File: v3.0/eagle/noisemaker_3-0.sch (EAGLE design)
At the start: 57 parts, among them IC1 REG1117, U3 ATMEGA32U4, Y1 16MHz

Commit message: board updates...
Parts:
- NPN: device transistor:-NPN-TO220V -> SparkFun-DiscreteSemi:TRANSISTOR_NPNSOT23-3
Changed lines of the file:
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@@
 <part name="R8" library="SparkFun-Passives" deviceset="RESISTOR" device="1206"/>
 <part name="R9" library="SparkFun-Passives" deviceset="RESISTOR" device="1206"/>
-<part name="NPN" library="transistor" deviceset="*-NPN-" device="TO220V"/>
+<part name="NPN" library="SparkFun-DiscreteSemi" deviceset="TRANSISTOR_NPN" device="SOT23-3"/>
 <part name="GND16" library="supply1" deviceset="GND" device=""/>
 <part name="AMP-" library="SparkFun-Connectors" deviceset="M01" device="PTH_LONGPAD"/>

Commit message: updated board layout
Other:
- moved on the sheet: AMP+, AMP-, JP4, NPN, PH1, PH2, PH3, R11, R15, R19, R20, R3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

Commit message: updated board layout tues
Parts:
- added JP8: M01PTH_LONGPAD, SparkFun-Connectors:M01PTH_LONGPAD
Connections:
- net VCC: now also JP8.1
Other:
- note added: "sensor1"
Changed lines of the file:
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@@
 <part name="P+12" library="SparkFun" deviceset="3.3V" device="" value="VCC"/>
 <part name="P+14" library="SparkFun" deviceset="3.3V" device="" value="VCC"/>
+<part name="JP8" library="SparkFun-Connectors" deviceset="M01" device="PTH_LONGPAD" value="M01PTH_LONGPAD"/>
 </parts>
 <sheets>
@@
 <text x="220.98" y="27.94" size="1.778" layer="94" ratio="10">power</text>
 <text x="263.144" y="174.752" size="1.778" layer="94">Gadgiteration Noisemaker v3.0</text>
+<text x="205.74" y="154.94" size="1.778" layer="94">sensor1</text>
+<text x="205.74" y="152.4" size="1.778" layer="94">sensor1</text>
+<text x="205.74" y="149.86" size="1.778" layer="94">sensor1</text>
 </plain>
 <instances>
@@
 <attribute name="VALUE" x="40.64" y="47.244" size="1.778" layer="96" rot="R180"/>
 </instance>
+<instance part="JP8" gate="G$1" x="114.3" y="162.56" rot="R180"/>
 </instances>
 <busses>
@@
 <wire x1="68.58" y1="154.94" x2="68.58" y2="162.56" width="0.1524" layer="91"/>
 <junction x="68.58" y="162.56"/>
-</segment>
-<segment>
+<pinref part="JP8" gate="G$1" pin="1"/>
+<wire x1="106.68" y1="162.56" x2="99.06" y2="162.56" width="0.1524" layer="91"/>
+</segment>
+<segment>

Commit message: merging in @shanqiu's latest updates
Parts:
- removed PH3: M9960_11B, photo-elements:M9960_11B
- removed R20: (no value), SparkFun-Passives:RESISTOR1206
- added JP9, LED_STRIP: (no value), pinhead:PINHD-1X3/90
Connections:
- new net N$11: LED_STRIP.3
- new net N$6: LED_STRIP.1
- net A4: now also JP9.2; no longer PH3.2, R20.2
- net D6: now also LED_STRIP.2
- net GND: now also JP9.3; no longer R20.1
- net VCC: now also JP9.1; no longer PH3.1
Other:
- note added: "audio"
- note added: "human circuit pole"
- note added: "led"
- note added: "led _strip"
- note added: "leds(human circuit/ regular circuit)"
- note added: "mode button"
- note added: "range button"
- note added: "regular circuit pole"
- note added: "sensor1(2 legs)"
- note added: "sensor2(2 legs)"
- note added: "sensor3(3 legs)"
- note removed: "sensor1"
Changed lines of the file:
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@@
 <?xml version="1.0" encoding="utf-8"?>
 <!DOCTYPE eagle SYSTEM "eagle.dtd">
-<eagle version="6.4">
+<eagle version="6.5.0">
 <drawing>
 <settings>
@@
 <part name="R15" library="SparkFun-Passives" deviceset="RESISTOR" device="1206"/>
 <part name="R19" library="SparkFun-Passives" deviceset="RESISTOR" device="1206"/>
-<part name="R20" library="SparkFun-Passives" deviceset="RESISTOR" device="1206"/>
 <part name="PH2" library="photo-elements" deviceset="M9960_11" device="" technology="B"/>
-<part name="PH3" library="photo-elements" deviceset="M9960_11" device="" technology="B"/>
 <part name="GND21" library="supply1" deviceset="GND" device=""/>
 <part name="P+3" library="SparkFun" deviceset="3.3V" device="" value="VCC"/>
@@
 <part name="P+14" library="SparkFun" deviceset="3.3V" device="" value="VCC"/>
 <part name="JP8" library="SparkFun-Connectors" deviceset="M01" device="PTH_LONGPAD" value="M01PTH_LONGPAD"/>
+<part name="JP9" library="pinhead" deviceset="PINHD-1X3" device="/90"/>
+<part name="LED_STRIP" library="pinhead" deviceset="PINHD-1X3" device="/90"/>
+<part name="GND13" library="SparkFun" deviceset="GND" device=""/>
+<part name="P+8" library="SparkFun" deviceset="3.3V" device="" value="VCC"/>
 </parts>
 <sheets>
@@
 <text x="220.98" y="27.94" size="1.778" layer="94" ratio="10">power</text>
 <text x="263.144" y="174.752" size="1.778" layer="94">Gadgiteration Noisemaker v3.0</text>
-<text x="205.74" y="154.94" size="1.778" layer="94">sensor1</text>
-<text x="205.74" y="152.4" size="1.778" layer="94">sensor1</text>
-<text x="205.74" y="149.86" size="1.778" layer="94">sensor1</text>
+<text x="205.74" y="147.32" size="1.778" layer="94">sensor3(3 legs)</text>
+<text x="205.74" y="152.4" size="1.778" layer="94">sensor1(2 legs)</text>
+<text x="205.74" y="149.86" size="1.778" layer="94">sensor2(2 legs)</text>
+<text x="205.74" y="154.94" size="1.778" layer="94">human circuit pole</text>
+<text x="205.74" y="157.48" size="1.778" layer="94">regular circuit pole</text>
+<text x="205.74" y="129.54" size="1.778" layer="94">mode button</text>
+<text x="205.74" y="124.46" size="1.778" layer="94">range button</text>
+<text x="205.74" y="114.3" size="1.778" layer="94">audio</text>
+<text x="205.74" y="116.84" size="1.778" layer="94">leds(human circuit/ regular circuit)</text>
+<text x="205.74" y="96.52" size="1.778" layer="94">led</text>
+<text x="205.74" y="119.38" size="1.778" layer="94">led _strip</text>
+<text x="198.12" y="86.36" size="1.778" layer="94">led</text>
 </plain>
 <instances>
@@
 <instance part="R15" gate="G$1" x="243.84" y="116.84"/>
 <instance part="R19" gate="G$1" x="243.84" y="111.76"/>
-<instance part="R20" gate="G$1" x="243.84" y="106.68"/>
 <instance part="PH2" gate="G$1" x="274.32" y="121.92"/>
-<instance part="PH3" gate="G$1" x="297.18" y="116.84"/>
 <instance part="GND21" gate="1" x="233.68" y="137.16" rot="R180"/>
 <instance part="P+3" gate="G$1" x="109.22" y="60.96" smashed="yes" rot="R270">
@@
 </instance>
 <instance part="JP8" gate="G$1" x="114.3" y="162.56" rot="R180"/>
+<instance part="JP9" gate="A" x="304.8" y="106.68"/>
+<instance part="LED_STRIP" gate="A" x="274.32" y="78.74"/>
+<instance part="GND13" gate="1" x="241.3" y="76.2" rot="R270"/>
+<instance part="P+8" gate="G$1" x="243.84" y="81.28" smashed="yes" rot="R90">
+<attribute name="VALUE" x="237.998" y="78.994" size="1.778" layer="96" rot="R90"/>
+</instance>
 </instances>
 <busses>
@@
 </segment>
 <segment>
-<pinref part="R20" gate="G$1" pin="1"/>
-<wire x1="238.76" y1="106.68" x2="233.68" y2="106.68" width="0.1524" layer="91"/>
-<wire x1="233.68" y1="106.68" x2="233.68" y2="111.76" width="0.1524" layer="91"/>
 <pinref part="R19" gate="G$1" pin="1"/>
 <wire x1="233.68" y1="111.76" x2="233.68" y2="116.84" width="0.1524" layer="91"/>
@@
 <junction x="233.68" y="116.84"/>
 <pinref part="GND21" gate="1" pin="GND"/>
+<pinref part="JP9" gate="A" pin="3"/>
+<wire x1="233.68" y1="104.14" x2="233.68" y2="111.76" width="0.1524" layer="91"/>
+<wire x1="302.26" y1="104.14" x2="233.68" y2="104.14" width="0.1524" layer="91"/>
 </segment>
 <segment>
@@
 <segment>
 <pinref part="PH1" gate="G$1" pin="1"/>
-<pinref part="PH3" gate="G$1" pin="1"/>
 <wire x1="251.46" y1="132.08" x2="274.32" y2="132.08" width="0.1524" layer="91"/>
 <wire x1="274.32" y1="132.08" x2="297.18" y2="132.08" width="0.1524" layer="91"/>
-<wire x1="297.18" y1="132.08" x2="297.18" y2="121.92" width="0.1524" layer="91"/>
 <pinref part="PH2" gate="G$1" pin="1"/>
 <wire x1="274.32" y1="127" x2="274.32" y2="132.08" width="0.1524" layer="91"/>
 <junction x="274.32" y="132.08"/>
 <pinref part="P+7" gate="G$1" pin="3.3V"/>
+<pinref part="JP9" gate="A" pin="1"/>
+<wire x1="302.26" y1="109.22" x2="297.18" y2="109.22" width="0.1524" layer="91"/>
+<wire x1="297.18" y1="109.22" x2="297.18" y2="132.08" width="0.1524" layer="91"/>
 </segment>
 <segment>
@@
 </segment>
 <segment>
-<pinref part="R20" gate="G$1" pin="2"/>
-<wire x1="248.92" y1="106.68" x2="297.18" y2="106.68" width="0.1524" layer="91"/>
-<pinref part="PH3" gate="G$1" pin="2"/>
-<wire x1="297.18" y1="106.68" x2="307.34" y2="106.68" width="0.1524" layer="91"/>
-<wire x1="297.18" y1="111.76" x2="297.18" y2="106.68" width="0.1524" layer="91"/>
-<junction x="297.18" y="106.68"/>
-<label x="302.26" y="106.68" size="1.778" layer="95"/>
+<wire x1="302.26" y1="106.68" x2="314.96" y2="106.68" width="0.1524" layer="91"/>
+<label x="314.96" y="106.68" size="1.778" layer="95"/>
+<pinref part="JP9" gate="A" pin="2"/>
 </segment>
 </net>
@@
 <pinref part="U3" gate="G$1" pin="PD7(ADC10)"/>
 </segment>
+<segment>
+<pinref part="LED_STRIP" gate="A" pin="2"/>
+<wire x1="271.78" y1="78.74" x2="246.38" y2="78.74" width="0.1524" layer="91"/>
+<label x="246.38" y="78.74" size="1.778" layer="95"/>
+</segment>
 </net>
 <net name="D7" class="0">
@@
 <wire x1="162.56" y1="20.32" x2="149.86" y2="20.32" width="0.1524" layer="91"/>
 <junction x="162.56" y="20.32"/>
-<label x="144.78" y="20.32" size="1.778" layer="95"/>
+<label x="142.24" y="20.32" size="1.778" layer="95"/>
 </segment>
 </net>
@@
 </segment>
 </net>
+<net name="N$6" class="0">
+<segment>
+<pinref part="LED_STRIP" gate="A" pin="1"/>
+<wire x1="271.78" y1="81.28" x2="243.84" y2="81.28" width="0.1524" layer="91"/>
+</segment>
+</net>
+<net name="N$11" class="0">
+<segment>
+<pinref part="LED_STRIP" gate="A" pin="3"/>
+<wire x1="271.78" y1="76.2" x2="243.84" y2="76.2" width="0.1524" layer="91"/>
+<pinref part="GND13" gate="1" pin="GND"/>
+<junction x="243.84" y="76.2"/>
+</segment>
+</net>

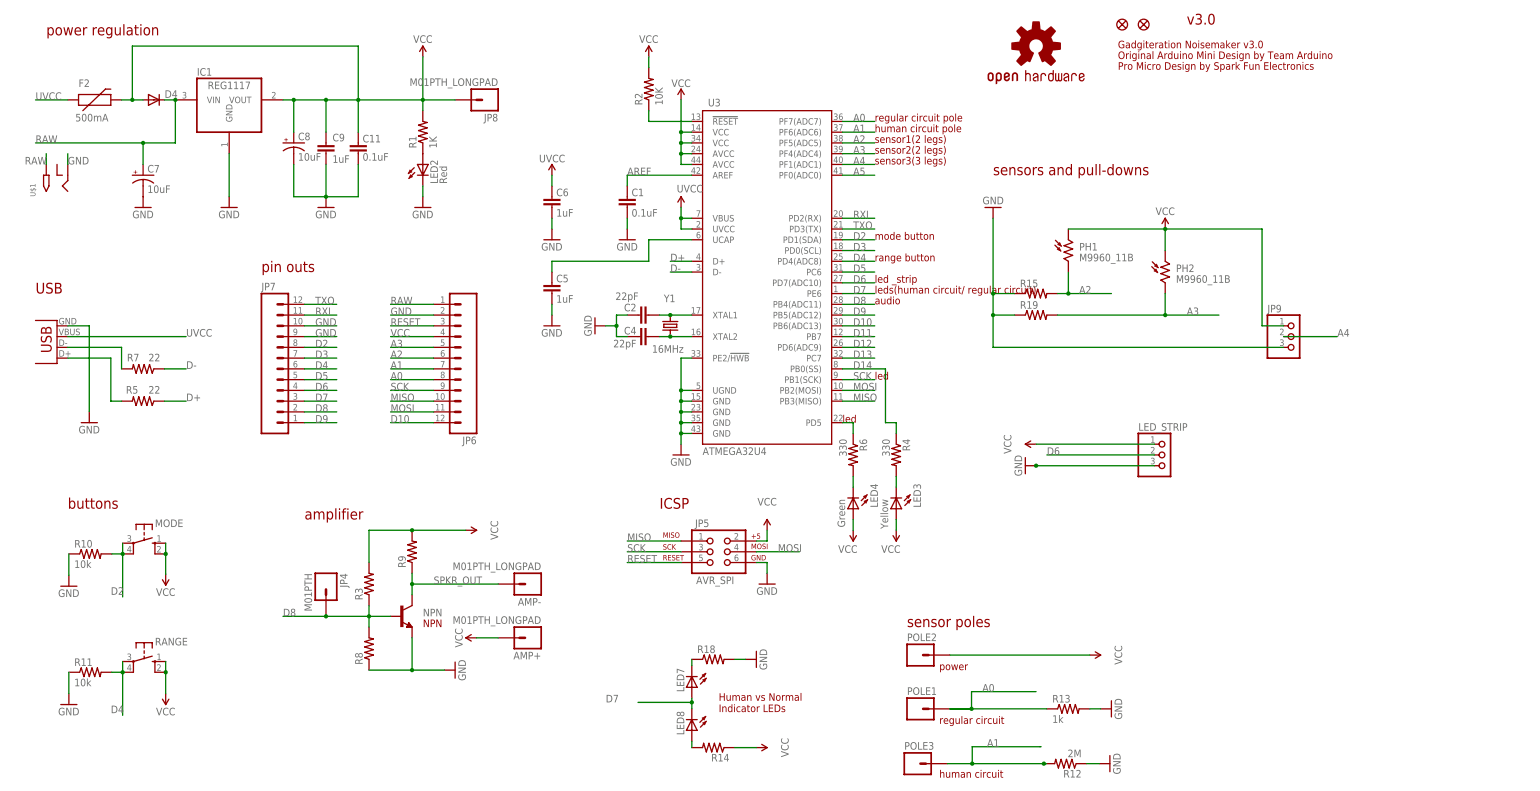
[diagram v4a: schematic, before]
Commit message: board file
text has been updated, layout is completed. needs logos, names, more text love.
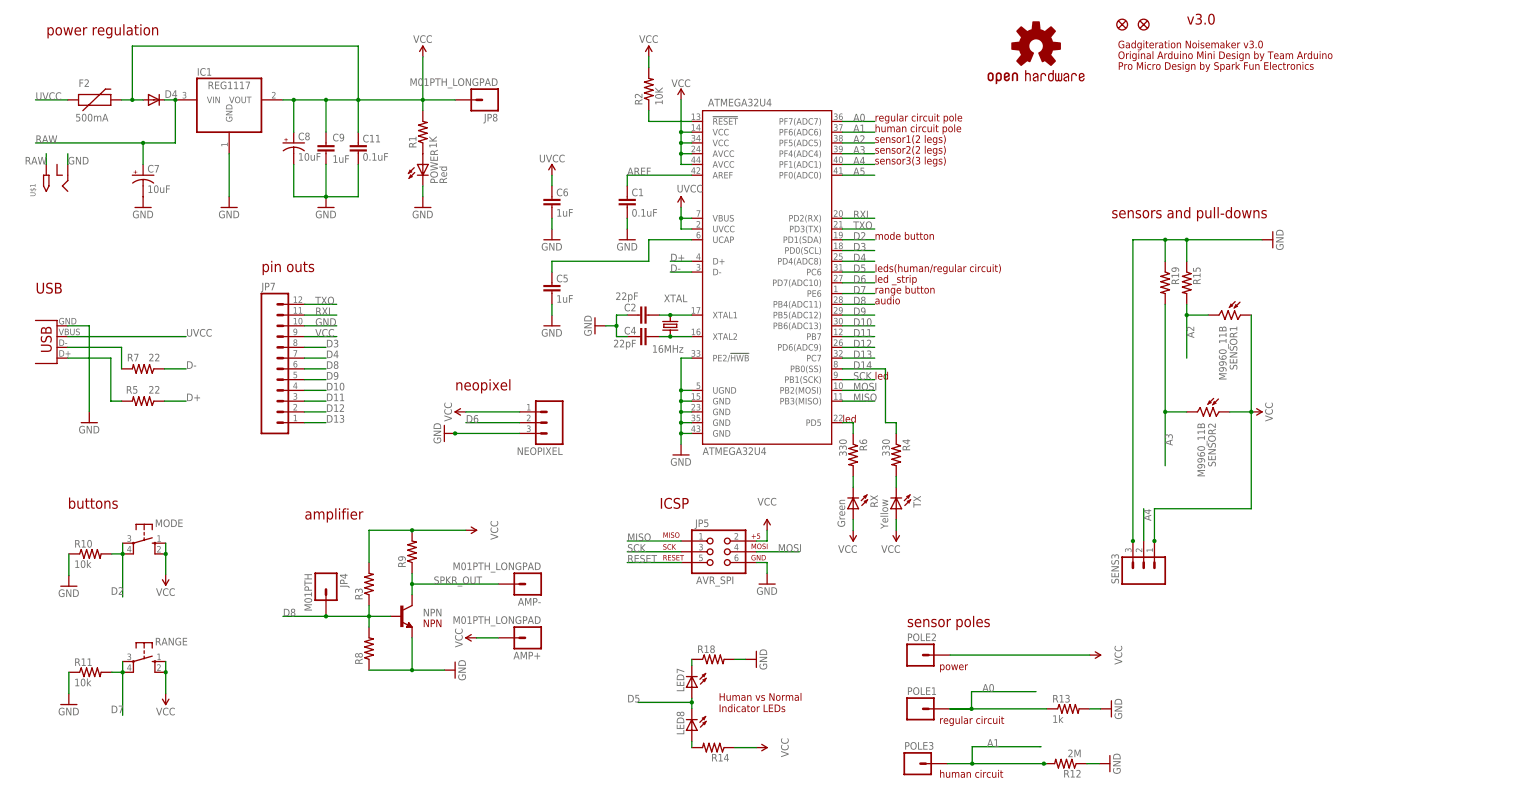
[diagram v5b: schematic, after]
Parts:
- removed JP6: M12PTH, SparkFun:M12PTH
- removed JP9, LED_STRIP: (no value), pinhead:PINHD-1X3/90
- removed PH1, PH2: M9960_11B, photo-elements:M9960_11B
- added NEOPIXEL: (no value), SparkFun-Connectors:M03LONGPADS
- added SENS3: (no value), SparkFun-Connectors:M03POGO_PIN_HOLES_ONLY
- added SENSOR1, SENSOR2: M9960_11B, photo-elements:M9960_11B
- renumbered LED2 to POWER, LED3 to TX, LED4 to RX, U3 to ATMEGA32U4, Y1 to XTAL
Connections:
- removed net N$11: LED_STRIP.3
- removed net N$6: LED_STRIP.1
- net A0: no longer JP6.8
- net A1: no longer JP6.7
- net A2: now also SENSOR1.2; no longer JP6.6, PH1.2
- net A3: now also SENSOR2.2; no longer JP6.5, PH2.2
- net A4: now also SENS3.2; no longer JP9.2
- net D10: now also JP7.4; no longer JP6.12
- net D11: now also JP7.3
- net D12: now also JP7.2
- net D13: now also JP7.1
- net D2: no longer JP7.8
- net D3: now also JP7.8; no longer JP7.7
- net D4: now also JP7.7; no longer JP7.6, R11.2, RANGE.P, RANGE.P1
- net D5: now also LED7.A, LED8.C; no longer JP7.5
- net D6: now also NEOPIXEL.2; no longer JP7.4, LED_STRIP.2
- net D7: now also R11.2, RANGE.P, RANGE.P1; no longer JP7.3, LED7.A, LED8.C
- net D8: now also JP7.6; no longer JP7.2
- net D9: now also JP7.5; no longer JP7.1
- net GND: now also NEOPIXEL.3, SENS3.3; no longer JP6.2, JP7.9, JP9.3
- net MISO: no longer JP6.10
- net MOSI: no longer JP6.11
- net RAW: no longer JP6.1
- net RESET: no longer JP6.3
- net SCK: no longer JP6.9
- net VCC: now also JP7.9, NEOPIXEL.1, SENS3.1, SENSOR1.1, SENSOR2.1; no longer JP6.4, JP9.1, PH1.1, PH2.1
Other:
- note added: "leds(human/regular circuit)"
- note added: "neopixel"
- note removed: "leds(human circuit/ regular circuit)"
- moved on the sheet: R15, R19
